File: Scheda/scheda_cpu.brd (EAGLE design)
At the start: 56.8 x 67.3 mm, 23 parts, among them IC2 7805, IC3 LD1117V33

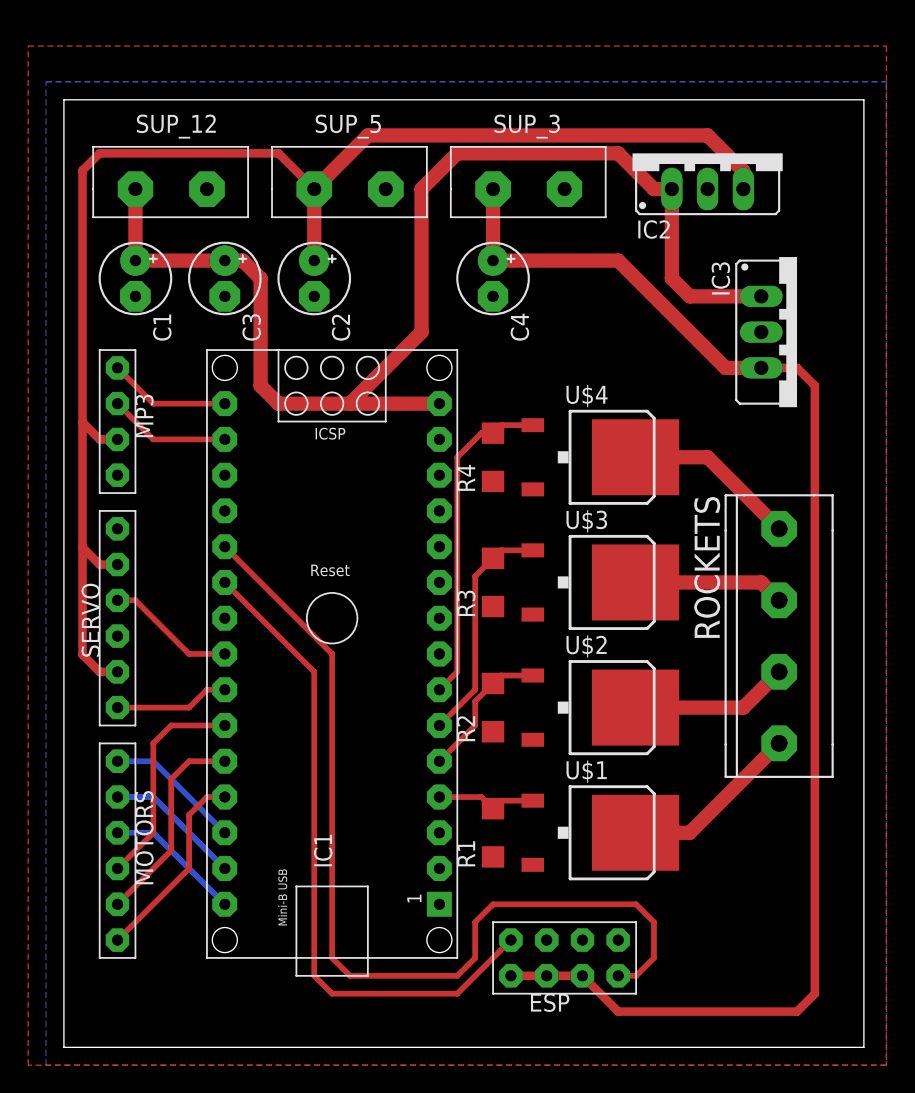
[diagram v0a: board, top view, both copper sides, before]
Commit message: modificato il sistema di accensione
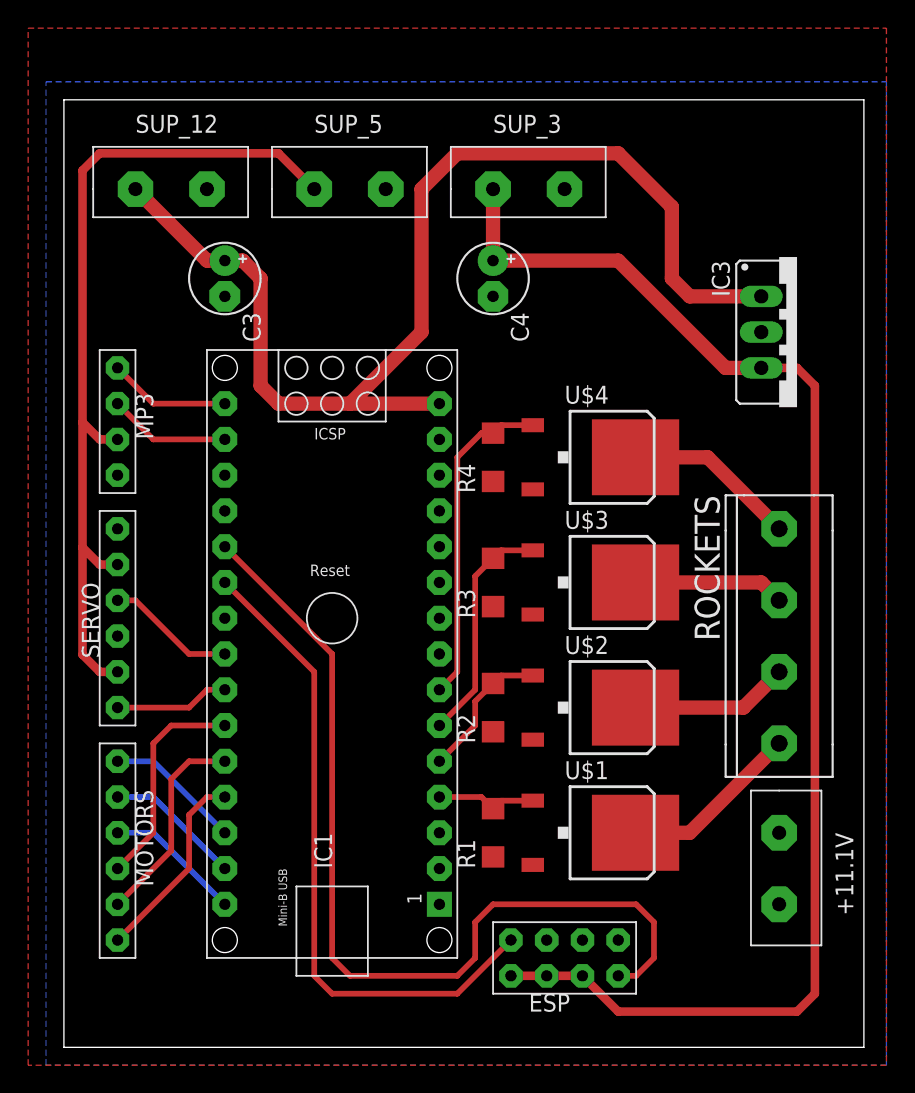
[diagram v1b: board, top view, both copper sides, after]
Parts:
- removed C1, C2: (no value), roombarmato_eagle_lib:E2,5-5
- removed IC2: 7805, roombarmato_eagle_lib:78XXS
- added +11.1V: AK500, roombarmato_eagle_lib:AK500-2
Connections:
- net +12V: now also +11.1V.P$1, +11.1V.P$2; no longer C1.+, IC2.IN
- net +5V: no longer C2.+, IC2.OUT
- net GND: no longer C1.-, C2.-, IC2.GND
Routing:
- net +5V: track 100.9 -> 61.4 mm
- net +12V: track 85.8 -> 82.1 mm
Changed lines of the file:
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@@
 </autorouter>
 <elements>
-<element name="C1" library="roombarmato_eagle_lib" package="E2,5-5" value="" x="5.08" y="54.61" smashed="yes" rot="R270">
-<attribute name="NAME" x="6.35" y="52.197" size="1.27" layer="25" ratio="10" rot="R270"/>
-<attribute name="VALUE" x="2.667" y="52.197" size="1.27" layer="27" ratio="10" rot="R270"/>
-</element>
-<element name="C2" library="roombarmato_eagle_lib" package="E2,5-5" value="" x="17.78" y="54.61" smashed="yes" rot="R270">
-<attribute name="NAME" x="19.05" y="52.197" size="1.27" layer="25" ratio="10" rot="R270"/>
-<attribute name="VALUE" x="15.367" y="52.197" size="1.27" layer="27" ratio="10" rot="R270"/>
-</element>
 <element name="C3" library="roombarmato_eagle_lib" package="E2,5-5" value="" x="11.43" y="54.61" smashed="yes" rot="R270">
 <attribute name="NAME" x="12.7" y="52.197" size="1.27" layer="25" ratio="10" rot="R270"/>
@@
 <element name="IC1" library="roombarmato_eagle_lib" package="ARDUINO_NANO" package3d_urn="urn:adsk.eagle:package:16064398/3" value="" x="19.05" y="30.48" smashed="yes" rot="R90">
 <attribute name="NAME" x="19.05" y="12.7" size="1.27" layer="21" font="vector" rot="R90"/>
-</element>
-<element name="IC2" library="roombarmato_eagle_lib" package="78XXS" value="7805" x="45.72" y="63.5" smashed="yes">
-<attribute name="NAME" x="40.64" y="57.4548" size="1.27" layer="25" ratio="10"/>
-<attribute name="VALUE" x="40.64" y="55.88" size="1.27" layer="27" ratio="10"/>
 </element>
 <element name="IC3" library="roombarmato_eagle_lib" package="78XXS" value="LD1117V33" x="52.07" y="50.8" smashed="yes" rot="R270">
@@
 <attribute name="NAME" x="44.8" y="39.21" size="1.778" layer="25" rot="R270"/>
 </element>
+<element name="+11.1V" library="roombarmato_eagle_lib" package="AK500-2" package3d_urn="urn:adsk.eagle:package:17855270/2" value="AK500" x="50.8" y="15.24" smashed="yes" rot="R270">
+<attribute name="NAME" x="54.8" y="15.24" size="1.27" layer="25" rot="R270"/>
+</element>
 </elements>
 <signals>
@@
 <contactref element="IC1" pad="15"/>
 <contactref element="SUP_12" pad="P$1"/>
-<contactref element="IC2" pad="IN"/>
-<contactref element="C1" pad="+"/>
 <contactref element="IC3" pad="IN"/>
 <contactref element="C3" pad="+"/>
-<wire x1="5.08" y1="60.96" x2="5.08" y2="55.88" width="1.016" layer="1"/>
-<wire x1="5.08" y1="55.88" x2="11.43" y2="55.88" width="1.016" layer="1"/>
-<wire x1="43.18" y1="60.96" x2="43.18" y2="54.61" width="1.016" layer="1"/>
 <wire x1="43.18" y1="54.61" x2="44.45" y2="53.34" width="1.016" layer="1"/>
 <wire x1="44.45" y1="53.34" x2="49.53" y2="53.34" width="1.016" layer="1"/>
-<wire x1="11.43" y1="55.88" x2="12.7" y2="55.88" width="1.016" layer="1"/>
-<wire x1="12.7" y1="55.88" x2="13.97" y2="54.61" width="1.016" layer="1"/>
-<wire x1="13.97" y1="54.61" x2="13.97" y2="46.99" width="1.016" layer="1"/>
+<wire x1="13.97" y1="46.99" x2="13.97" y2="54.61" width="1.016" layer="1"/>
 <wire x1="13.97" y1="46.99" x2="15.24" y2="45.72" width="1.016" layer="1"/>
 <wire x1="15.24" y1="45.72" x2="20.32" y2="45.72" width="1.016" layer="1"/>
-<wire x1="20.32" y1="45.72" x2="26.67" y2="45.72" width="1.016" layer="1"/>
-<wire x1="43.18" y1="60.96" x2="41.91" y2="60.96" width="1.016" layer="1"/>
-<wire x1="39.37" y1="63.5" x2="27.94" y2="63.5" width="1.016" layer="1"/>
-<wire x1="27.94" y1="63.5" x2="25.4" y2="60.96" width="1.016" layer="1"/>
-<wire x1="25.4" y1="60.96" x2="25.4" y2="50.8" width="1.016" layer="1"/>
-<wire x1="25.4" y1="50.8" x2="20.32" y2="45.72" width="1.016" layer="1"/>
-<wire x1="41.91" y1="60.96" x2="39.37" y2="63.5" width="1.016" layer="1"/>
+<wire x1="26.67" y1="45.72" x2="20.32" y2="45.72" width="1.016" layer="1"/>
+<wire x1="20.32" y1="45.72" x2="25.4" y2="50.8" width="1.016" layer="1"/>
+<wire x1="25.4" y1="50.8" x2="25.4" y2="60.96" width="1.016" layer="1"/>
+<wire x1="25.4" y1="60.96" x2="27.94" y2="63.5" width="1.016" layer="1"/>
+<wire x1="39.37" y1="63.5" x2="43.18" y2="59.69" width="1.016" layer="1"/>
+<wire x1="43.18" y1="59.69" x2="43.18" y2="54.61" width="1.016" layer="1"/>
+<wire x1="27.94" y1="63.5" x2="39.37" y2="63.5" width="1.016" layer="1"/>
+<wire x1="13.97" y1="54.61" x2="12.7" y2="55.88" width="1.016" layer="1"/>
+<wire x1="12.7" y1="55.88" x2="11.43" y2="55.88" width="1.016" layer="1"/>
+<wire x1="11.43" y1="55.88" x2="10.16" y2="55.88" width="1.016" layer="1"/>
+<wire x1="10.16" y1="55.88" x2="5.08" y2="60.96" width="1.016" layer="1"/>
+<contactref element="+11.1V" pad="P$1"/>
+<contactref element="+11.1V" pad="P$2"/>
+<wire x1="50.8" y1="10.16" x2="50.8" y2="15.24" width="0" layer="19" extent="1-1"/>
+<wire x1="49.53" y1="53.34" x2="50.8" y2="15.24" width="0" layer="19" extent="1-1"/>
 </signal>
 <signal name="GND" airwireshidden="yes">
@@
 <contactref element="U$1" pad="3"/>
 <contactref element="R1" pad="P$1"/>
-<contactref element="IC2" pad="GND"/>
-<contactref element="C1" pad="-"/>
-<contactref element="C2" pad="-"/>
 <contactref element="C3" pad="-"/>
 <contactref element="IC3" pad="GND"/>
@@
 <vertex x="58.42" y="-1.27"/>
 <vertex x="-2.54" y="-1.27"/>
-<vertex x="-2.54" y="71.12"/>
-<vertex x="58.42" y="71.12"/>
+<vertex x="-2.54" y="72.39"/>
+<vertex x="58.42" y="72.39"/>
 </polygon>
 </signal>
@@
 <contactref element="SERVO" pad="P$5"/>
 <contactref element="SUP_5" pad="P$1"/>
-<contactref element="IC2" pad="OUT"/>
-<contactref element="C2" pad="+"/>
-<wire x1="17.78" y1="60.96" x2="17.78" y2="55.88" width="1.016" layer="1"/>
-<wire x1="17.78" y1="60.96" x2="21.59" y2="64.77" width="1.016" layer="1"/>
-<wire x1="45.72" y1="64.77" x2="48.26" y2="62.23" width="1.016" layer="1"/>
-<wire x1="48.26" y1="62.23" x2="48.26" y2="60.96" width="1.016" layer="1"/>
-<wire x1="21.59" y1="64.77" x2="45.72" y2="64.77" width="1.016" layer="1"/>
 <wire x1="3.81" y1="43.18" x2="2.54" y2="43.18" width="0.6096" layer="1"/>
 <wire x1="2.54" y1="43.18" x2="1.3208" y2="44.3992" width="0.6096" layer="1"/>

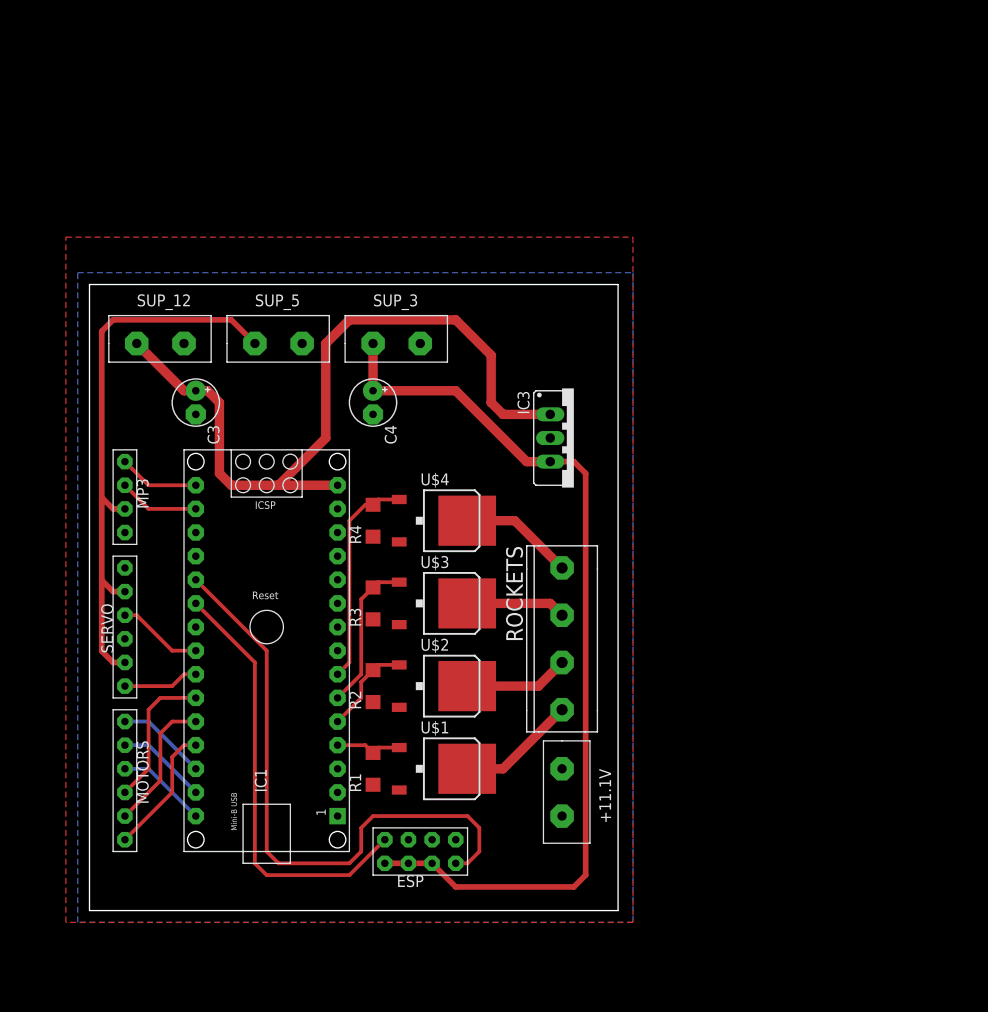
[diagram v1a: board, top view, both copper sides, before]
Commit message: completato pcb con lm380
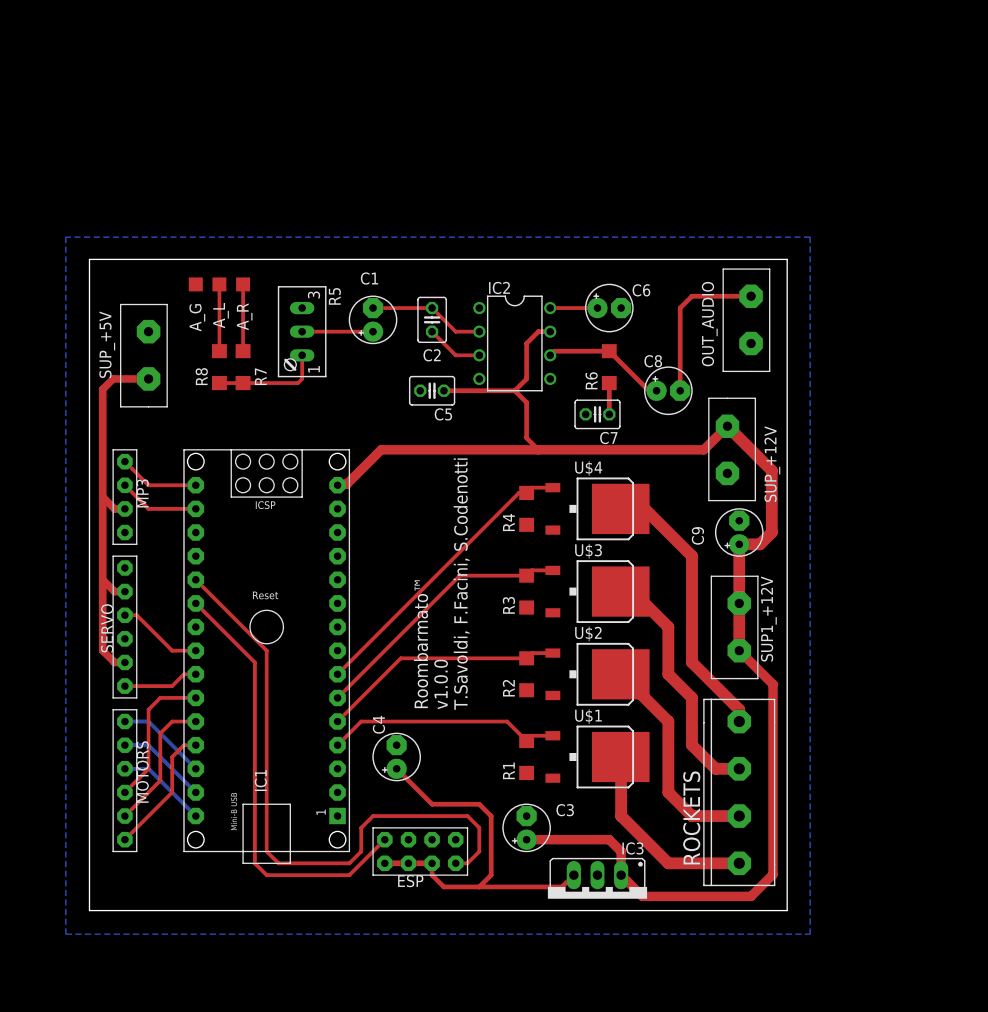
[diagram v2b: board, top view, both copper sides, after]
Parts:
- removed +11.1V, SUP_12, SUP_3, SUP_5: AK500, roombarmato_eagle_lib:AK500-2
- added A_G, A_L, A_R: TPTP15SQ, testpad:TP15SQ
- added C1, C6: 10uF, roombarmato_eagle_lib:E2,5-5
- added C2: 4.7nF, ITIS:C025-030X050
- added C5, C7: 100nF, ITIS:C025-030X050
- added C8, C9: 470uF, roombarmato_eagle_lib:E2,5-5
- added IC2: LM3801N, roombarmato_eagle_lib:DIL08
- added OUT_AUDIO, SUP1_+12V, SUP_+12V, SUP_+5V: AK500, roombarmato_eagle_lib:AK500-2
- added R5: (no value), pot:S64W
- added R6: 2.7, roombarmato_eagle_lib:1206-RESISTOR
- added R7, R8: 100, roombarmato_eagle_lib:1206-RESISTOR
- moved C3 57.9 mm to (47.0, 8.89), turned to 90 degrees
- moved IC3 49.6 mm to (54.6, 1.27), turned to 180 degrees
- moved C4 38.2 mm to (33.0, 16.5), turned to 90 degrees
- moved ROCKETS 25.2 mm to (69.8, 12.7)
- moved R1 16.6 mm to (47.0, 16.5)
- moved R2 16.6 mm to (47.0, 25.4)
- moved R3 16.6 mm to (47.0, 34.3)
- moved R4 16.6 mm to (47.0, 43.2)
- moved U$1 16.6 mm to (54.6, 16.5)
- moved U$2 16.6 mm to (54.6, 25.4)
- moved U$3 16.6 mm to (54.6, 34.3)
- moved U$4 16.6 mm to (54.6, 43.2)
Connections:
- new net IN_AUDIO: R5.A, R7.P$2, R8.P$2
- new net N$10: C8.+, IC2.6, R6.P$2
- new net N$17: C8.-, OUT_AUDIO.P$2
- new net N$18: A_R.TP, R7.P$1
- new net N$19: A_L.TP, R8.P$1
- new net N$5: C1.+, R5.S
- new net N$6: C1.-, C2.1, IC2.2
- new net N$7: C2.2, IC2.3
- new net N$8: C6.+, IC2.8
- new net N$9: C7.1, R6.P$1
- net +12V: now also C5.1, C9.+, IC2.7, SUP1_+12V.P$1, SUP1_+12V.P$2, SUP_+12V.P$1; no longer +11.1V.P$1, +11.1V.P$2, SUP_12.P$1
- net +3.3V: no longer SUP_3.P$1
- net +5V: now also SUP_+5V.P$1; no longer SUP_5.P$1
- net GND: now also A_G.TP, C5.2, C6.-, C7.2, C9.-, IC2.5, OUT_AUDIO.P$1, R5.E, SUP_+12V.P$2, SUP_+5V.P$2; no longer SUP_12.P$2, SUP_3.P$2, SUP_5.P$2
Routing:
- net +12V: track 82.1 -> 154.1 mm
- net +3.3V: track 98.0 -> 43.1 mm
- net R2: track 10.7 -> 30.1 mm
- net +5V: track 61.4 -> 42.2 mm
- net R3: track 12.3 -> 31.4 mm
- net C_R0: track 7.21 -> 25.3 mm
- net N$17: track 0.00 -> 17.0 mm
- net C_R1: track 10.2 -> 26.2 mm
- net N$10: track 0.00 -> 13.4 mm
- net N$6: track 0.00 -> 12.5 mm
- net C_R2: track 16.5 -> 28.8 mm
- net R1: track 11.3 -> 23.5 mm
- net IN_AUDIO: track 0.00 -> 11.6 mm
- net R0: track 12.8 -> 21.2 mm
- net C_R3: track 24.2 -> 31.8 mm
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- removed copper zone on layer 1, net GND
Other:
- board size 56.8 x 67.3 mm -> 75 x 70 mm
- board text added: "Roombarmato™ v1.0.0 T.Savoldi, F.Facini, S.Codenotti"

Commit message: creato file excel ordine
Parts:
- C1, C6: device roombarmato_eagle_lib:E2,5-5 -> ITIS:E2-4
- C8: device roombarmato_eagle_lib:E2,5-5 -> ITIS:E3,5-8
- C9: value 470uF -> 1000uF; device roombarmato_eagle_lib:E2,5-5 -> ITIS:E3,5-10
- R5: value (none) -> 10k
- moved SUP_+12V 3.59 mm to (71.1, 49.5), turned to 90 degrees
- moved C2 2.54 mm to (36.8, 61.0)
- moved C1 1.27 mm to (30.5, 62.2), turned to 0 degrees
- moved SUP1_+12V 1.27 mm to (69.8, 26.7)
- moved C8 1.27 mm to (62.2, 57.1)
- moved C9 1.27 mm to (68.6, 40.6)
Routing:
- net +12V: track 154.1 -> 149.9 mm
- net N$6: track 12.5 -> 10.4 mm
- net N$17: track 17.0 -> 15.6 mm
- net N$7: track 6.13 -> 5.08 mm
- net N$10: track 13.4 -> 12.3 mm
- net N$5: track 7.62 -> 6.60 mm
